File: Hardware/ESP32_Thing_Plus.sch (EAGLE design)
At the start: 33 parts, among them J1 455-1750-1-ND, J2 USB Female Type C Connector, J3 AUDIO_JACK_TRRSSMD_RA, Q2 MBT3904DW1T1, U1 I2SMICMIC, U2 ESP-WROOM-32NARROW, U3 AP2112K-3.3V, U4 CP2102N

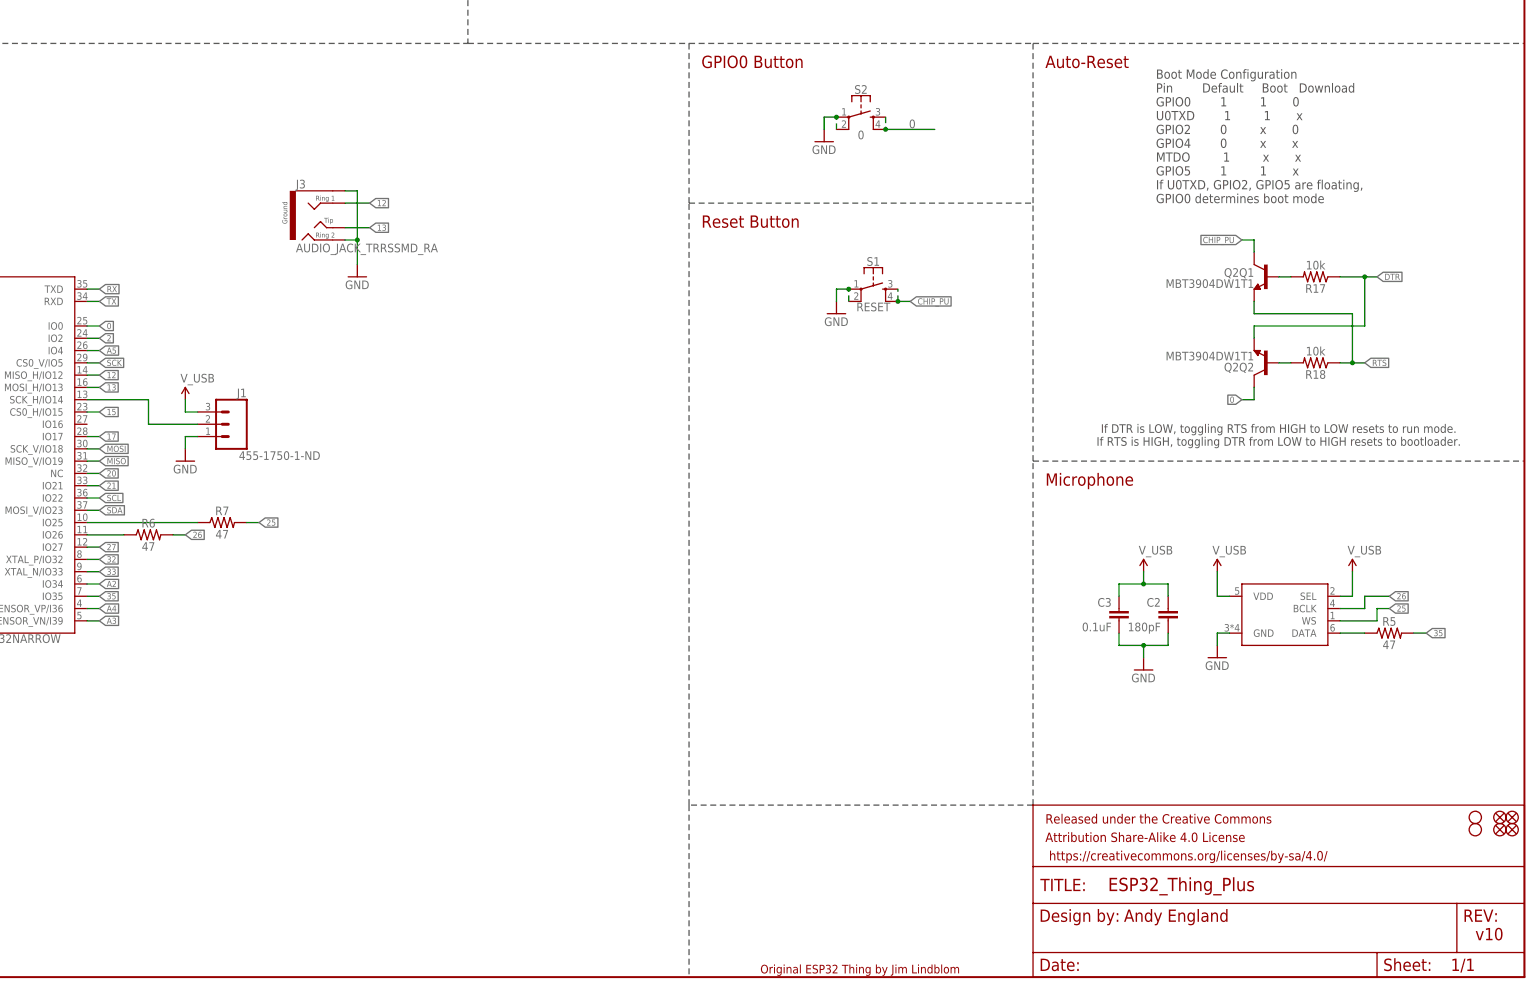
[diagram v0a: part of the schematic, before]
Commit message: updating mic and trrs circuits
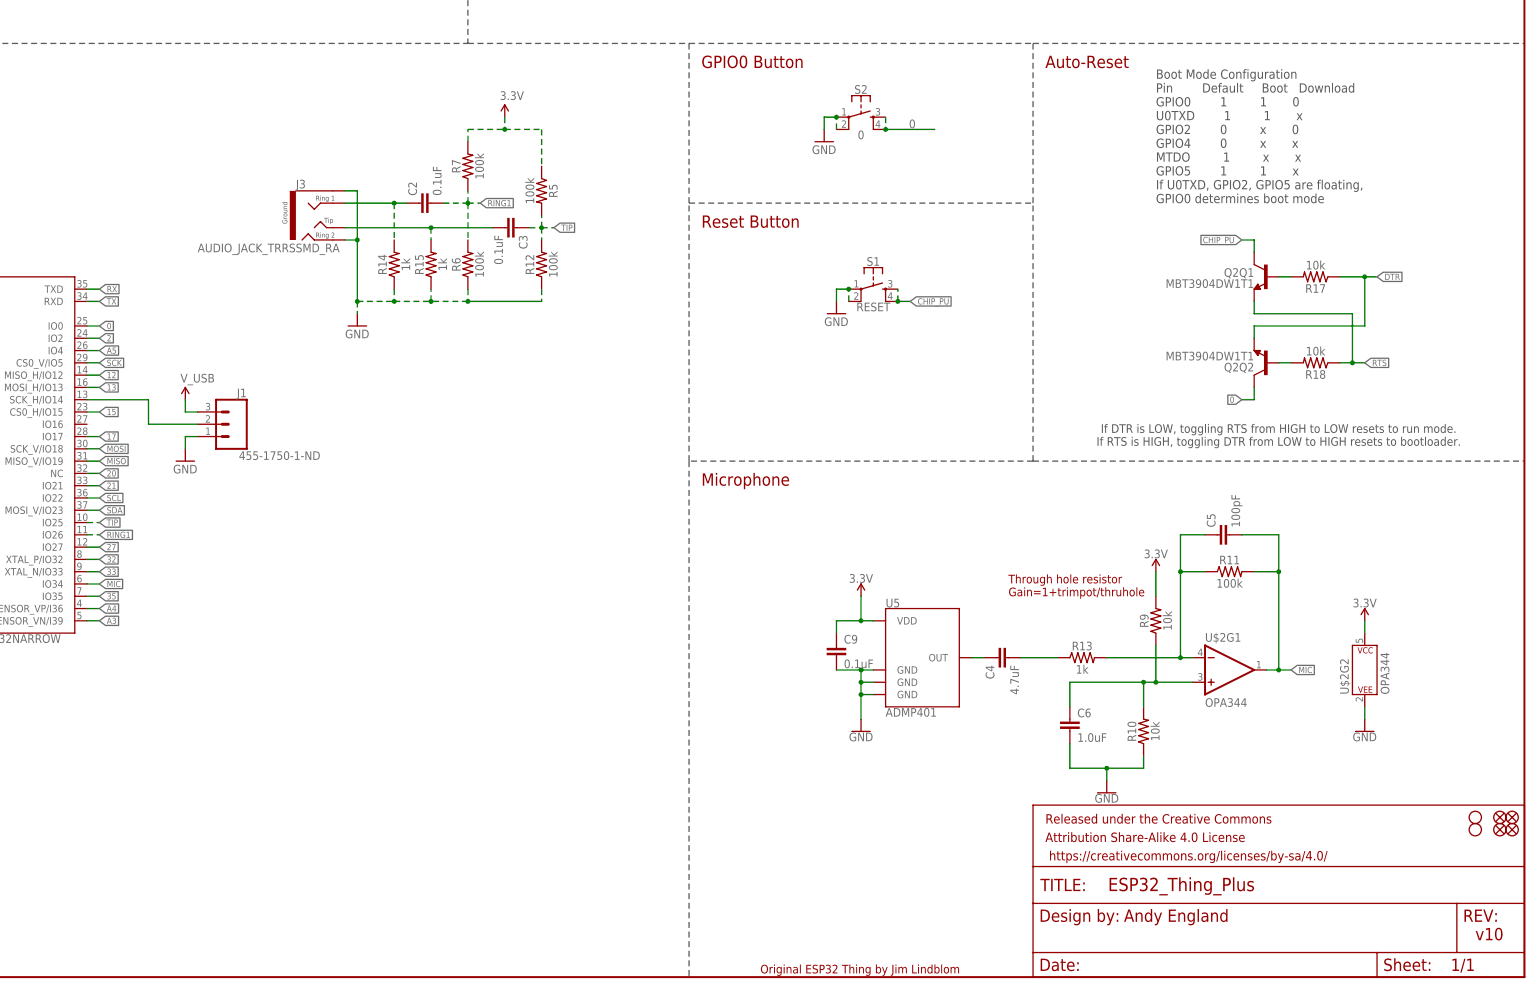
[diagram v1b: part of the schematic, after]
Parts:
- removed U1: I2SMICMIC, Andy:I2SMICMIC
- added C4: 4.7uF, SparkFun-Capacitors:4.7UF-0603-6.3V-(10%)
- added C5: 100pF, SparkFun-Capacitors:100PF-0603-50V-5%
- added C6: 1.0uF, SparkFun-Capacitors:1.0UF-0603-16V-10%
- added C9: 0.1uF, SparkFun-Capacitors:0.1UF-0603-25V-5%
- added R10, R9: 10k, SparkFun-Resistors:10KOHM-0603-1/10W-1%
- added R11, R12: 100k, SparkFun-Resistors:100KOHM-0603-1/10W-1%
- added R13: 1k, SparkFun-Resistors:1KOHM-HORIZ-1/4W-5%
- added R14, R15: 1k, SparkFun-Resistors:1KOHM-0603-1/10W-1%
- added U$2: OPA344, SparkFun-IC-Amplifiers:OPA344
- added U5: ADMP401, SparkFun-Sensors:ADMP401
- C2: value 180pF -> 0.1uF; device SparkFun-Capacitors:180PF-0603-50V-5% -> SparkFun-Capacitors:0.1UF-0603-25V-5%
- C3: device SparkFun-Capacitors:0.1UF-0603-25V-(+80/-20%) -> SparkFun-Capacitors:0.1UF-0603-25V-5%
- R5, R6, R7: value 47 -> 100k; device SparkFun-Resistors:47OHM-0603-1/10W-1% -> SparkFun-Resistors:100KOHM-0603-1/10W-1%
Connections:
- removed net 25: R7.2, U1.WS
- removed net 26: R6.2, U1.BCLK
- removed net A2: U2.IO34
- removed net N$8: R7.1, U2.IO25
- new net MIC: C5.2, R11.2, U$2G1.OUT, U2.IO34
- new net N$11: C4.2, R13.1
- new net N$16: C6.1, R10.2, R9.1, U$2G1.+IN
- new net N$5: C4.1, U5.OUT
- new net N$9: C5.1, R11.1, R13.2, U$2G1.-IN
- new net RING1: C2.2, R6.2, R7.1, U2.IO26
- new net TIP: C3.1, R12.2, R5.2, U2.IO25
- net 12: no longer J3.RING1
- net 13: no longer J3.TIP
- net 3.3V: now also C9.1, R5.1, R7.2, R9.2, U$2G2.P$V+, U5.VDD
- net 35: no longer R5.2
- net GND: now also C6.2, C9.2, R10.1, R12.1, R14.1, R15.1, R6.1, U$2G2.P$V-, U5.GND@2, U5.GND@4, U5.GND@6; no longer C2.2, C3.2, U1.GND
- net N$6: now also C3.2, J3.TIP, R15.2; no longer R5.1, U1.DATA
- net N$7: now also C2.1, J3.RING1, R14.2; no longer R6.1, U2.IO26
- net V_USB: no longer C2.1, C3.1, U1.SEL, U1.VDD
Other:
- note added: "Through hole resistor Gain=1+trimpot/thruhole"
- moved on the sheet: C2, C3

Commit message: partially through layout
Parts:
- removed J1: 455-1750-1-ND, SparkFun-Connectors:CONN_03
- added D1, D10, D100, D101, D102, D103, D104, D105, D106, D107, D108, D109, D11, D110, D111, D112, D113, D114, D115, D116, D117, D118, D119, D12, D120, D121, D122, D123, D124, D125, D126, D127, D128, D129, D13, D130, D131, D132, D133, D134, D135, D136, D137, D138, D139, D14, D140, D141, D142, D143, D144, D145, D146, D147, D148, D149, D15, D150, D151, D152, D153, D154, D155, D156, D157, D158, D159, D16, D160, D161, D162, D163, D164, D165, D166, D167, D168, D169, D17, D170, D171, D172, D173, D174, D175, D176, D177, D178, D179, D18, D180, D181, D182, D183, D184, D185, D186, D187, D188, D189, D19, D190, D191, D192, D193, D194, D195, D196, D197, D198, D199, D2, D20, D200, D201, D202, D203, D204, D205, D206, D207, D208, D209, D21, D210, D211, D212, D213, D214, D215, D216, D217, D218, D219, D22, D220, D221, D222, D223, D224, D225, D226, D227, D228, D229, D23, D230, D231, D232, D233, D234, D235, D236, D237, D238, D239, D24, D240, D241, D242, D243, D244, D245, D246, D247, D248, D249, D25, D250, D251, D252, D253, D254, D255, D256, D257, D258, D259, D26, D260, D261, D262, D263, D27, D28, D29, D3, D30, D31, D32, D33, D34, D35, D36, D37, D38, D39, D4, D40, D41, D42, D43, D44, D45, D46, D47, D48, D49, D5, D50, D51, D52, D53, D54, D55, D56, D57, D58, D59, D6, D60, D61, D62, D63, D64, D65, D66, D67, D68, D69, D7, D70, D71, D72, D73, D74, D75, D76, D77, D78, D79, D8, D80, D81, D82, D83, D84, D85, D86, D87, D88, D89, D9, D90, D91, D92, D93, D94, D95, D96, D97, D98, D99: WS2812B, SparkFun-LED:WS2812B
- added FRAME2, FRAME3, FRAME4: FRAME-LEDGER, SparkFun-Aesthetics:FRAME-LEDGER
- added JP1, JP10, JP100, JP101, JP102, JP103, JP104, JP105, JP106, JP107, JP108, JP109, JP11, JP110, JP111, JP112, JP113, JP114, JP115, JP116, JP117, JP118, JP119, JP12, JP120, JP121, JP122, JP123, JP124, JP125, JP126, JP127, JP128, JP129, JP13, JP130, JP131, JP132, JP133, JP134, JP135, JP136, JP137, JP138, JP139, JP14, JP140, JP141, JP142, JP143, JP144, JP145, JP146, JP147, JP148, JP149, JP15, JP150, JP151, JP152, JP153, JP154, JP155, JP156, JP157, JP158, JP159, JP16, JP160, JP161, JP162, JP163, JP164, JP165, JP166, JP167, JP168, JP169, JP17, JP170, JP171, JP172, JP173, JP174, JP175, JP176, JP177, JP178, JP179, JP18, JP180, JP181, JP182, JP183, JP184, JP185, JP186, JP187, JP188, JP189, JP19, JP190, JP191, JP192, JP193, JP194, JP195, JP196, JP197, JP198, JP199, JP2, JP20, JP200, JP201, JP202, JP203, JP204, JP205, JP206, JP207, JP208, JP209, JP21, JP210, JP211, JP212, JP213, JP214, JP215, JP216, JP217, JP218, JP219, JP22, JP220, JP221, JP222, JP223, JP224, JP225, JP226, JP227, JP228, JP229, JP23, JP230, JP231, JP232, JP233, JP234, JP235, JP236, JP237, JP238, JP239, JP24, JP240, JP241, JP242, JP243, JP244, JP245, JP246, JP247, JP248, JP249, JP25, JP250, JP251, JP252, JP253, JP254, JP255, JP256, JP257, JP258, JP259, JP26, JP260, JP261, JP262, JP263, JP27, JP28, JP29, JP3, JP30, JP31, JP32, JP33, JP34, JP35, JP36, JP37, JP38, JP39, JP4, JP40, JP41, JP42, JP43, JP44, JP45, JP46, JP47, JP48, JP49, JP5, JP50, JP51, JP52, JP53, JP54, JP55, JP56, JP57, JP58, JP59, JP6, JP60, JP61, JP62, JP63, JP64, JP65, JP66, JP67, JP68, JP69, JP7, JP70, JP71, JP72, JP73, JP74, JP75, JP76, JP77, JP78, JP79, JP8, JP80, JP81, JP82, JP83, JP84, JP85, JP86, JP87, JP88, JP89, JP9, JP90, JP91, JP92, JP93, JP94, JP95, JP96, JP97, JP98, JP99: JUMPER-SMT_2_NO_NO-SILK, SparkFun-Jumpers:JUMPER-SMT_2_NO_NO-SILK
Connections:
- new net DIO0: D1.DI, JP1.1, U2.SCK_H/IO14
- new net DIO1: D100.DI, D101.DO, D102.DI, D99.DO, JP100.1, JP101.2, JP102.1, JP99.2
- new net DIO10: D21.DO, D22.DI, JP21.2, JP22.1
- new net DIO100: D191.DO, D192.DI, JP191.2, JP192.1
- new net DIO101: D193.DO, D194.DI, JP193.2, JP194.1
- new net DIO102: D195.DO, D196.DI, JP195.2, JP196.1
- new net DIO103: D197.DO, D198.DI, JP197.2, JP198.1
- new net DIO104: D209.DO, D210.DI, JP209.2, JP210.1
- new net DIO105: D202.DO, D203.DI, JP202.2, JP203.1
- new net DIO106: D204.DO, D205.DI, JP204.2, JP205.1
- new net DIO107: D206.DO, D207.DI, JP206.2, JP207.1
- new net DIO108: D208.DO, D209.DI, JP208.2, JP209.1
- new net DIO109: D211.DO, D212.DI, JP211.2, JP212.1
- new net DIO11: D22.DO, D23.DI, JP22.2, JP23.1
- new net DIO110: D213.DO, D214.DI, JP213.2, JP214.1
- new net DIO111: D215.DO, D216.DI, JP215.2, JP216.1
- new net DIO112: D217.DO, D218.DI, JP217.2, JP218.1
- new net DIO113: D219.DO, D220.DI, JP219.2, JP220.1
- new net DIO114: D220.DO, D221.DI, JP220.2, JP221.1
- new net DIO115: D222.DO, D223.DI, JP222.2, JP223.1
- new net DIO116: D224.DO, D225.DI, JP224.2, JP225.1
- new net DIO117: D226.DO, D227.DI, JP226.2, JP227.1
- new net DIO118: D228.DO, D229.DI, JP228.2, JP229.1
- new net DIO119: D230.DO, D231.DI, JP230.2, JP231.1
- new net DIO12: D24.DO, D25.DI, JP24.2, JP25.1
- new net DIO120: D231.DO, JP231.2
- new net DIO121: D232.DI, JP232.1
- new net DIO122: D233.DO, D234.DI, JP233.2, JP234.1
- new net DIO123: D235.DO, D236.DI, JP235.2, JP236.1
- new net DIO124: D237.DO, D238.DI, JP237.2, JP238.1
- new net DIO125: D239.DO, D240.DI, JP239.2, JP240.1
- new net DIO126: D241.DO, D242.DI, JP241.2, JP242.1
- new net DIO128: D242.DO, D243.DI, JP242.2, JP243.1
- new net DIO129: D244.DO, D245.DI, JP244.2, JP245.1
- new net DIO13: D26.DO, D27.DI, JP26.2, JP27.1
- new net DIO130: D246.DO, D247.DI, JP246.2, JP247.1
- new net DIO131: D248.DO, D249.DI, JP248.2, JP249.1
- new net DIO132: D250.DO, D251.DI, JP250.2, JP251.1
- new net DIO133: D252.DO, D253.DI, JP252.2, JP253.1
- new net DIO134: D253.DO, D254.DI, JP253.2, JP254.1
- new net DIO135: D255.DO, D256.DI, JP255.2, JP256.1
- new net DIO136: D257.DO, D258.DI, JP257.2, JP258.1
- new net DIO137: D259.DO, D260.DI, JP259.2, JP260.1
- new net DIO138: D261.DO, D262.DI, JP261.2, JP262.1
- new net DIO139: D263.DO, JP263.2
- new net DIO14: D28.DO, D29.DI, JP28.2, JP29.1
- new net DIO15: D30.DO, D31.DI, JP30.2, JP31.1
- new net DIO16: D32.DO, D33.DI, JP32.2, JP33.1
- new net DIO17: D33.DO, D34.DI, JP33.2, JP34.1
- new net DIO18: D35.DO, D36.DI, JP35.2, JP36.1
- new net DIO19: D37.DO, D38.DI, JP37.2, JP38.1
- new net DIO2: D198.DO, D199.DI, JP198.2, JP199.1
- new net DIO20: D39.DO, D40.DI, JP39.2, JP40.1
- new net DIO21: D41.DO, D42.DI, JP41.2, JP42.1
- new net DIO22: D43.DO, D44.DI, JP43.2, JP44.1
- new net DIO23: D44.DO, D45.DI, JP44.2, JP45.1
- new net DIO24: D46.DO, D47.DI, JP46.2, JP47.1
- new net DIO25: D48.DO, D49.DI, JP48.2, JP49.1
- new net DIO26: D50.DO, D51.DI, JP50.2, JP51.1
- new net DIO27: D52.DO, D53.DI, JP52.2, JP53.1
- new net DIO28: D54.DO, D55.DI, JP54.2, JP55.1
- new net DIO29: D55.DO, D56.DI, JP55.2, JP56.1
- new net DIO3: D6.DO, D7.DI, JP6.2, JP7.1
- new net DIO30: D57.DO, D58.DI, JP57.2, JP58.1
- new net DIO31: D59.DO, D60.DI, JP59.2, JP60.1
- new net DIO32: D61.DO, D62.DI, JP61.2, JP62.1
- new net DIO33: D63.DO, D64.DI, JP63.2, JP64.1
- new net DIO34: D65.DO, D66.DI, JP65.2, JP66.1
- new net DIO35: D66.DO, D67.DI, JP66.2, JP67.1
- new net DIO36: D68.DO, D69.DI, JP68.2, JP69.1
- new net DIO37: D70.DO, D71.DI, JP70.2, JP71.1
- new net DIO38: D72.DO, D73.DI, JP72.2, JP73.1
- new net DIO39: D74.DO, D75.DI, JP74.2, JP75.1
- new net DIO4: D8.DO, D9.DI, JP8.2, JP9.1
- new net DIO40: D76.DO, D77.DI, JP76.2, JP77.1
- new net DIO41: D77.DO, D78.DI, JP77.2, JP78.1
- new net DIO42: D79.DO, D80.DI, JP79.2, JP80.1
- new net DIO43: D81.DO, D82.DI, JP81.2, JP82.1
- new net DIO44: D83.DO, D84.DI, JP83.2, JP84.1
- new net DIO45: D85.DO, D86.DI, JP85.2, JP86.1
- new net DIO46: D87.DO, D88.DI, JP87.2, JP88.1
- new net DIO47: D88.DO, D89.DI, JP88.2, JP89.1
- new net DIO48: D90.DO, D91.DI, JP90.2, JP91.1
- new net DIO49: D92.DO, D93.DI, JP92.2, JP93.1
- new net DIO5: D10.DO, D11.DI, JP10.2, JP11.1
- new net DIO50: D94.DO, D95.DI, JP94.2, JP95.1
- new net DIO51: D96.DO, D97.DI, JP96.2, JP97.1
- new net DIO52: D98.DO, D99.DI, JP98.2, JP99.1
- new net DIO53: D103.DO, D104.DI, JP103.2, JP104.1
- new net DIO54: D105.DO, D106.DI, JP105.2, JP106.1
- new net DIO55: D107.DO, D108.DI, JP107.2, JP108.1
- new net DIO56: D109.DO, D110.DI, JP109.2, JP110.1
- new net DIO57: D112.DO, D113.DI, JP112.2, JP113.1
- new net DIO58: D114.DO, D115.DI, JP114.2, JP115.1
- new net DIO59: D116.DO, D117.DI, JP116.2, JP117.1
- new net DIO6: D13.DO, D14.DI, JP13.2, JP14.1
- new net DIO60: D118.DO, D119.DI, JP118.2, JP119.1
- new net DIO61: D120.DO, D121.DI, JP120.2, JP121.1
- new net DIO62: D121.DO, D122.DI, JP121.2, JP122.1
- new net DIO63: D123.DO, D124.DI, JP123.2, JP124.1
- new net DIO64: D125.DO, D126.DI, JP125.2, JP126.1
- new net DIO65: D127.DO, D128.DI, JP127.2, JP128.1
- new net DIO66: D129.DO, D130.DI, JP129.2, JP130.1
- new net DIO67: D131.DO, D132.DI, JP131.2, JP132.1
- new net DIO68: D132.DO, D133.DI, JP132.2, JP133.1
- new net DIO69: D134.DO, D135.DI, JP134.2, JP135.1
- new net DIO7: D15.DO, D16.DI, JP15.2, JP16.1
- new net DIO70: D136.DO, D137.DI, JP136.2, JP137.1
- new net DIO71: D138.DO, D139.DI, JP138.2, JP139.1
- new net DIO72: D140.DO, D141.DI, JP140.2, JP141.1
- new net DIO73: D142.DO, D143.DI, JP142.2, JP143.1
- new net DIO74: D143.DO, D144.DI, JP143.2, JP144.1
- new net DIO75: D145.DO, D146.DI, JP145.2, JP146.1
- new net DIO76: D147.DO, D148.DI, JP147.2, JP148.1
- new net DIO77: D149.DO, D150.DI, JP149.2, JP150.1
- new net DIO78: D151.DO, D152.DI, JP151.2, JP152.1
- new net DIO79: D153.DO, D154.DI, JP153.2, JP154.1
- new net DIO8: D17.DO, D18.DI, JP17.2, JP18.1
- new net DIO80: D154.DO, D155.DI, JP154.2, JP155.1
- new net DIO81: D156.DO, D157.DI, JP156.2, JP157.1
- new net DIO82: D158.DO, D159.DI, JP158.2, JP159.1
- new net DIO83: D160.DO, D161.DI, JP160.2, JP161.1
- new net DIO84: D162.DO, D163.DI, JP162.2, JP163.1
- new net DIO85: D164.DO, D165.DI, JP164.2, JP165.1
- new net DIO86: D165.DO, D166.DI, JP165.2, JP166.1
- new net DIO87: D167.DO, D168.DI, JP167.2, JP168.1
- new net DIO88: D169.DO, D170.DI, JP169.2, JP170.1
- new net DIO89: D171.DO, D172.DI, JP171.2, JP172.1
- new net DIO9: D19.DO, D20.DI, JP19.2, JP20.1
- new net DIO90: D173.DO, D174.DI, JP173.2, JP174.1
- new net DIO91: D175.DO, D176.DI, JP175.2, JP176.1
- new net DIO92: D176.DO, D177.DI, JP176.2, JP177.1
- new net DIO93: D178.DO, D179.DI, JP178.2, JP179.1
- new net DIO94: D180.DO, D181.DI, JP180.2, JP181.1
- new net DIO95: D182.DO, D183.DI, JP182.2, JP183.1
- new net DIO96: D184.DO, D185.DI, JP184.2, JP185.1
- new net DIO97: D186.DO, D187.DI, JP186.2, JP187.1
- new net DIO98: D187.DO, D188.DI, JP187.2, JP188.1
- new net DIO99: D189.DO, D190.DI, JP189.2, JP190.1
- new net N$100: D196.DO, D197.DI, JP196.2, JP197.1
- new net N$101: D194.DO, D195.DI, JP194.2, JP195.1
- new net N$102: D199.DO, D200.DI, JP199.2, JP200.1
- new net N$103: D203.DO, D204.DI, JP203.2, JP204.1
- new net N$104: D201.DO, D202.DI, JP201.2, JP202.1
- new net N$105: D207.DO, D208.DI, JP207.2, JP208.1
- new net N$106: D205.DO, D206.DI, JP205.2, JP206.1
- new net N$107: D210.DO, D211.DI, JP210.2, JP211.1
- new net N$108: D214.DO, D215.DI, JP214.2, JP215.1
- new net N$109: D212.DO, D213.DI, JP212.2, JP213.1
- new net N$110: D218.DO, D219.DI, JP218.2, JP219.1
- new net N$111: D216.DO, D217.DI, JP216.2, JP217.1
- new net N$112: D221.DO, D222.DI, JP221.2, JP222.1
- new net N$113: D225.DO, D226.DI, JP225.2, JP226.1
- new net N$114: D223.DO, D224.DI, JP223.2, JP224.1
- new net N$115: D229.DO, D230.DI, JP229.2, JP230.1
- new net N$116: D227.DO, D228.DI, JP227.2, JP228.1
- new net N$117: D232.DO, D233.DI, JP232.2, JP233.1
- new net N$118: D236.DO, D237.DI, JP236.2, JP237.1
- new net N$119: D234.DO, D235.DI, JP234.2, JP235.1
- new net N$120: D2.DO, D3.DI, JP2.2, JP3.1
- new net N$121: D4.DO, D5.DI, JP4.2, JP5.1
- new net N$122: D240.DO, D241.DI, JP240.2, JP241.1
- new net N$123: D238.DO, D239.DI, JP238.2, JP239.1
- new net N$124: D243.DO, D244.DI, JP243.2, JP244.1
- new net N$125: D247.DO, D248.DI, JP247.2, JP248.1
- new net N$126: D245.DO, D246.DI, JP245.2, JP246.1
- new net N$127: D251.DO, D252.DI, JP251.2, JP252.1
- new net N$128: D249.DO, D250.DI, JP249.2, JP250.1
- new net N$129: D254.DO, D255.DI, JP254.2, JP255.1
- new net N$13: D3.DO, D4.DI, JP3.2, JP4.1
- new net N$130: D258.DO, D259.DI, JP258.2, JP259.1
- new net N$131: D256.DO, D257.DI, JP256.2, JP257.1
- new net N$132: D262.DO, D263.DI, JP262.2, JP263.1
- new net N$133: D260.DO, D261.DI, JP260.2, JP261.1
- new net N$134: D110.DO, D111.DI, JP110.2, JP111.1
- new net N$135: D11.DO, D12.DI, JP11.2, JP12.1
- new net N$136: D200.DO, D201.DI, JP200.2, JP201.1
- new net N$14: D5.DO, D6.DI, JP5.2, JP6.1
- new net N$15: D10.DI, D9.DO, JP10.1, JP9.2
- new net N$17: D7.DO, D8.DI, JP7.2, JP8.1
- new net N$18: D16.DO, D17.DI, JP16.2, JP17.1
- new net N$19: D23.DO, D24.DI, JP23.2, JP24.1
- new net N$20: D14.DO, D15.DI, JP14.2, JP15.1
- new net N$21: D20.DO, D21.DI, JP20.2, JP21.1
- new net N$22: D18.DO, D19.DI, JP18.2, JP19.1
- new net N$23: D100.DO, D101.DI, JP100.2, JP101.1
- new net N$24: D27.DO, D28.DI, JP27.2, JP28.1
- new net N$25: D25.DO, D26.DI, JP25.2, JP26.1
- new net N$26: D31.DO, D32.DI, JP31.2, JP32.1
- new net N$27: D29.DO, D30.DI, JP29.2, JP30.1
- new net N$28: D104.DO, D105.DI, JP104.2, JP105.1
- new net N$29: D34.DO, D35.DI, JP34.2, JP35.1
- new net N$30: D38.DO, D39.DI, JP38.2, JP39.1
- new net N$31: D36.DO, D37.DI, JP36.2, JP37.1
- new net N$32: D42.DO, D43.DI, JP42.2, JP43.1
- new net N$33: D40.DO, D41.DI, JP40.2, JP41.1
- new net N$34: D45.DO, D46.DI, JP45.2, JP46.1
- new net N$35: D49.DO, D50.DI, JP49.2, JP50.1
- new net N$36: D47.DO, D48.DI, JP47.2, JP48.1
- new net N$37: D53.DO, D54.DI, JP53.2, JP54.1
- new net N$38: D51.DO, D52.DI, JP51.2, JP52.1
- new net N$39: D102.DO, D103.DI, JP102.2, JP103.1
- new net N$40: D56.DO, D57.DI, JP56.2, JP57.1
- new net N$41: D60.DO, D61.DI, JP60.2, JP61.1
- new net N$42: D58.DO, D59.DI, JP58.2, JP59.1
- new net N$43: D64.DO, D65.DI, JP64.2, JP65.1
- new net N$44: D62.DO, D63.DI, JP62.2, JP63.1
- new net N$45: D67.DO, D68.DI, JP67.2, JP68.1
- new net N$46: D71.DO, D72.DI, JP71.2, JP72.1
- new net N$47: D69.DO, D70.DI, JP69.2, JP70.1
- new net N$48: D75.DO, D76.DI, JP75.2, JP76.1
- new net N$49: D73.DO, D74.DI, JP73.2, JP74.1
- new net N$50: D78.DO, D79.DI, JP78.2, JP79.1
- new net N$51: D82.DO, D83.DI, JP82.2, JP83.1
- new net N$52: D80.DO, D81.DI, JP80.2, JP81.1
- new net N$53: D86.DO, D87.DI, JP86.2, JP87.1
- new net N$54: D84.DO, D85.DI, JP84.2, JP85.1
- new net N$55: D89.DO, D90.DI, JP89.2, JP90.1
- new net N$56: D93.DO, D94.DI, JP93.2, JP94.1
- new net N$57: D91.DO, D92.DI, JP91.2, JP92.1
- new net N$58: D97.DO, D98.DI, JP97.2, JP98.1
- new net N$59: D95.DO, D96.DI, JP95.2, JP96.1
- new net N$60: D108.DO, D109.DI, JP108.2, JP109.1
- new net N$61: D106.DO, D107.DI, JP106.2, JP107.1
- new net N$62: D111.DO, D112.DI, JP111.2, JP112.1
- new net N$63: D115.DO, D116.DI, JP115.2, JP116.1
- new net N$64: D113.DO, D114.DI, JP113.2, JP114.1
- new net N$65: D119.DO, D120.DI, JP119.2, JP120.1
- new net N$66: D117.DO, D118.DI, JP117.2, JP118.1
- new net N$67: D122.DO, D123.DI, JP122.2, JP123.1
- new net N$68: D126.DO, D127.DI, JP126.2, JP127.1
- new net N$69: D124.DO, D125.DI, JP124.2, JP125.1
- new net N$70: D130.DO, D131.DI, JP130.2, JP131.1
- new net N$71: D128.DO, D129.DI, JP128.2, JP129.1
- new net N$72: D133.DO, D134.DI, JP133.2, JP134.1
- new net N$73: D137.DO, D138.DI, JP137.2, JP138.1
- new net N$74: D135.DO, D136.DI, JP135.2, JP136.1
- new net N$75: D141.DO, D142.DI, JP141.2, JP142.1
- new net N$76: D139.DO, D140.DI, JP139.2, JP140.1
- new net N$77: D144.DO, D145.DI, JP144.2, JP145.1
- new net N$78: D148.DO, D149.DI, JP148.2, JP149.1
- new net N$79: D146.DO, D147.DI, JP146.2, JP147.1
- new net N$8: D12.DO, D13.DI, JP12.2, JP13.1
- new net N$80: D152.DO, D153.DI, JP152.2, JP153.1
- new net N$81: D150.DO, D151.DI, JP150.2, JP151.1
- new net N$82: D155.DO, D156.DI, JP155.2, JP156.1
- new net N$83: D159.DO, D160.DI, JP159.2, JP160.1
- new net N$84: D157.DO, D158.DI, JP157.2, JP158.1
- new net N$85: D163.DO, D164.DI, JP163.2, JP164.1
- new net N$86: D161.DO, D162.DI, JP161.2, JP162.1
- new net N$87: D166.DO, D167.DI, JP166.2, JP167.1
- new net N$88: D170.DO, D171.DI, JP170.2, JP171.1
- new net N$89: D168.DO, D169.DI, JP168.2, JP169.1
- new net N$90: D174.DO, D175.DI, JP174.2, JP175.1
- new net N$91: D172.DO, D173.DI, JP172.2, JP173.1
- new net N$92: D177.DO, D178.DI, JP177.2, JP178.1
- new net N$93: D181.DO, D182.DI, JP181.2, JP182.1
- new net N$94: D179.DO, D180.DI, JP179.2, JP180.1
- new net N$95: D185.DO, D186.DI, JP185.2, JP186.1
- new net N$96: D183.DO, D184.DI, JP183.2, JP184.1
- new net N$97: D188.DO, D189.DI, JP188.2, JP189.1
- new net N$98: D192.DO, D193.DI, JP192.2, JP193.1
- new net N$99: D190.DO, D191.DI, JP190.2, JP191.1
- net GND: now also D1.VSS, D10.VSS, D100.VSS, D101.VSS, D102.VSS, D103.VSS, D104.VSS, D105.VSS, D106.VSS, D107.VSS, D108.VSS, D109.VSS, D11.VSS, D110.VSS, D111.VSS, D112.VSS, D113.VSS, D114.VSS, D115.VSS, D116.VSS, D117.VSS, D118.VSS, D119.VSS, D12.VSS, D120.VSS, D121.VSS, D122.VSS, D123.VSS, D124.VSS, D125.VSS, D126.VSS, D127.VSS, D128.VSS, D129.VSS, D13.VSS, D130.VSS, D131.VSS, D132.VSS, D133.VSS, D134.VSS, D135.VSS, D136.VSS, D137.VSS, D138.VSS, D139.VSS, D14.VSS, D140.VSS, D141.VSS, D142.VSS, D143.VSS, D144.VSS, D145.VSS, D146.VSS, D147.VSS, D148.VSS, D149.VSS, D15.VSS, D150.VSS, D151.VSS, D152.VSS, D153.VSS, D154.VSS, D155.VSS, D156.VSS, D157.VSS, D158.VSS, D159.VSS, D16.VSS, D160.VSS, D161.VSS, D162.VSS, D163.VSS, D164.VSS, D165.VSS, D166.VSS, D167.VSS, D168.VSS, D169.VSS, D17.VSS, D170.VSS, D171.VSS, D172.VSS, D173.VSS, D174.VSS, D175.VSS, D176.VSS, D177.VSS, D178.VSS, D179.VSS, D18.VSS, D180.VSS, D181.VSS, D182.VSS, D183.VSS, D184.VSS, D185.VSS, D186.VSS, D187.VSS, D188.VSS, D189.VSS, D19.VSS, D190.VSS, D191.VSS, D192.VSS, D193.VSS, D194.VSS, D195.VSS, D196.VSS, D197.VSS, D198.VSS, D199.VSS, D2.VSS, D20.VSS, D200.VSS, D201.VSS, D202.VSS, D203.VSS, D204.VSS, D205.VSS, D206.VSS, D207.VSS, D208.VSS, D209.VSS, D21.VSS, D210.VSS, D211.VSS, D212.VSS, D213.VSS, D214.VSS, D215.VSS, D216.VSS, D217.VSS, D218.VSS, D219.VSS, D22.VSS, D220.VSS, D221.VSS, D222.VSS, D223.VSS, D224.VSS, D225.VSS, D226.VSS, D227.VSS, D228.VSS, D229.VSS, D23.VSS, D230.VSS, D231.VSS, D232.VSS, D233.VSS, D234.VSS, D235.VSS, D236.VSS, D237.VSS, D238.VSS, D239.VSS, D24.VSS, D240.VSS, D241.VSS, D242.VSS, D243.VSS, D244.VSS, D245.VSS, D246.VSS, D247.VSS, D248.VSS, D249.VSS, D25.VSS, D250.VSS, D251.VSS, D252.VSS, D253.VSS, D254.VSS, D255.VSS, D256.VSS, D257.VSS, D258.VSS, D259.VSS, D26.VSS, D260.VSS, D261.VSS, D262.VSS, D263.VSS, D27.VSS, D28.VSS, D29.VSS, D3.VSS, D30.VSS, D31.VSS, D32.VSS, D33.VSS, D34.VSS, D35.VSS, D36.VSS, D37.VSS, D38.VSS, D39.VSS, D4.VSS, D40.VSS, D41.VSS, D42.VSS, D43.VSS, D44.VSS, D45.VSS, D46.VSS, D47.VSS, D48.VSS, D49.VSS, D5.VSS, D50.VSS, D51.VSS, D52.VSS, D53.VSS, D54.VSS, D55.VSS, D56.VSS, D57.VSS, D58.VSS, D59.VSS, D6.VSS, D60.VSS, D61.VSS, D62.VSS, D63.VSS, D64.VSS, D65.VSS, D66.VSS, D67.VSS, D68.VSS, D69.VSS, D7.VSS, D70.VSS, D71.VSS, D72.VSS, D73.VSS, D74.VSS, D75.VSS, D76.VSS, D77.VSS, D78.VSS, D79.VSS, D8.VSS, D80.VSS, D81.VSS, D82.VSS, D83.VSS, D84.VSS, D85.VSS, D86.VSS, D87.VSS, D88.VSS, D89.VSS, D9.VSS, D90.VSS, D91.VSS, D92.VSS, D93.VSS, D94.VSS, D95.VSS, D96.VSS, D97.VSS, D98.VSS, D99.VSS; no longer J1.1
- net N$2: now also D1.DO, D2.DI, JP1.2, JP2.1; no longer J1.2, U2.SCK_H/IO14
- net V_USB: now also D1.VDD, D10.VDD, D100.VDD, D101.VDD, D102.VDD, D103.VDD, D104.VDD, D105.VDD, D106.VDD, D107.VDD, D108.VDD, D109.VDD, D11.VDD, D110.VDD, D111.VDD, D112.VDD, D113.VDD, D114.VDD, D115.VDD, D116.VDD, D117.VDD, D118.VDD, D119.VDD, D12.VDD, D120.VDD, D121.VDD, D122.VDD, D123.VDD, D124.VDD, D125.VDD, D126.VDD, D127.VDD, D128.VDD, D129.VDD, D13.VDD, D130.VDD, D131.VDD, D132.VDD, D133.VDD, D134.VDD, D135.VDD, D136.VDD, D137.VDD, D138.VDD, D139.VDD, D14.VDD, D140.VDD, D141.VDD, D142.VDD, D143.VDD, D144.VDD, D145.VDD, D146.VDD, D147.VDD, D148.VDD, D149.VDD, D15.VDD, D150.VDD, D151.VDD, D152.VDD, D153.VDD, D154.VDD, D155.VDD, D156.VDD, D157.VDD, D158.VDD, D159.VDD, D16.VDD, D160.VDD, D161.VDD, D162.VDD, D163.VDD, D164.VDD, D165.VDD, D166.VDD, D167.VDD, D168.VDD, D169.VDD, D17.VDD, D170.VDD, D171.VDD, D172.VDD, D173.VDD, D174.VDD, D175.VDD, D176.VDD, D177.VDD, D178.VDD, D179.VDD, D18.VDD, D180.VDD, D181.VDD, D182.VDD, D183.VDD, D184.VDD, D185.VDD, D186.VDD, D187.VDD, D188.VDD, D189.VDD, D19.VDD, D190.VDD, D191.VDD, D192.VDD, D193.VDD, D194.VDD, D195.VDD, D196.VDD, D197.VDD, D198.VDD, D199.VDD, D2.VDD, D20.VDD, D200.VDD, D201.VDD, D202.VDD, D203.VDD, D204.VDD, D205.VDD, D206.VDD, D207.VDD, D208.VDD, D209.VDD, D21.VDD, D210.VDD, D211.VDD, D212.VDD, D213.VDD, D214.VDD, D215.VDD, D216.VDD, D217.VDD, D218.VDD, D219.VDD, D22.VDD, D220.VDD, D221.VDD, D222.VDD, D223.VDD, D224.VDD, D225.VDD, D226.VDD, D227.VDD, D228.VDD, D229.VDD, D23.VDD, D230.VDD, D231.VDD, D232.VDD, D233.VDD, D234.VDD, D235.VDD, D236.VDD, D237.VDD, D238.VDD, D239.VDD, D24.VDD, D240.VDD, D241.VDD, D242.VDD, D243.VDD, D244.VDD, D245.VDD, D246.VDD, D247.VDD, D248.VDD, D249.VDD, D25.VDD, D250.VDD, D251.VDD, D252.VDD, D253.VDD, D254.VDD, D255.VDD, D256.VDD, D257.VDD, D258.VDD, D259.VDD, D26.VDD, D260.VDD, D261.VDD, D262.VDD, D263.VDD, D27.VDD, D28.VDD, D29.VDD, D3.VDD, D30.VDD, D31.VDD, D32.VDD, D33.VDD, D34.VDD, D35.VDD, D36.VDD, D37.VDD, D38.VDD, D39.VDD, D4.VDD, D40.VDD, D41.VDD, D42.VDD, D43.VDD, D44.VDD, D45.VDD, D46.VDD, D47.VDD, D48.VDD, D49.VDD, D5.VDD, D50.VDD, D51.VDD, D52.VDD, D53.VDD, D54.VDD, D55.VDD, D56.VDD, D57.VDD, D58.VDD, D59.VDD, D6.VDD, D60.VDD, D61.VDD, D62.VDD, D63.VDD, D64.VDD, D65.VDD, D66.VDD, D67.VDD, D68.VDD, D69.VDD, D7.VDD, D70.VDD, D71.VDD, D72.VDD, D73.VDD, D74.VDD, D75.VDD, D76.VDD, D77.VDD, D78.VDD, D79.VDD, D8.VDD, D80.VDD, D81.VDD, D82.VDD, D83.VDD, D84.VDD, D85.VDD, D86.VDD, D87.VDD, D88.VDD, D89.VDD, D9.VDD, D90.VDD, D91.VDD, D92.VDD, D93.VDD, D94.VDD, D95.VDD, D96.VDD, D97.VDD, D98.VDD, D99.VDD; no longer J1.3
